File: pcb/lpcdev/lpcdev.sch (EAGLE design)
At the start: 20 parts, among them Q1 16MHz

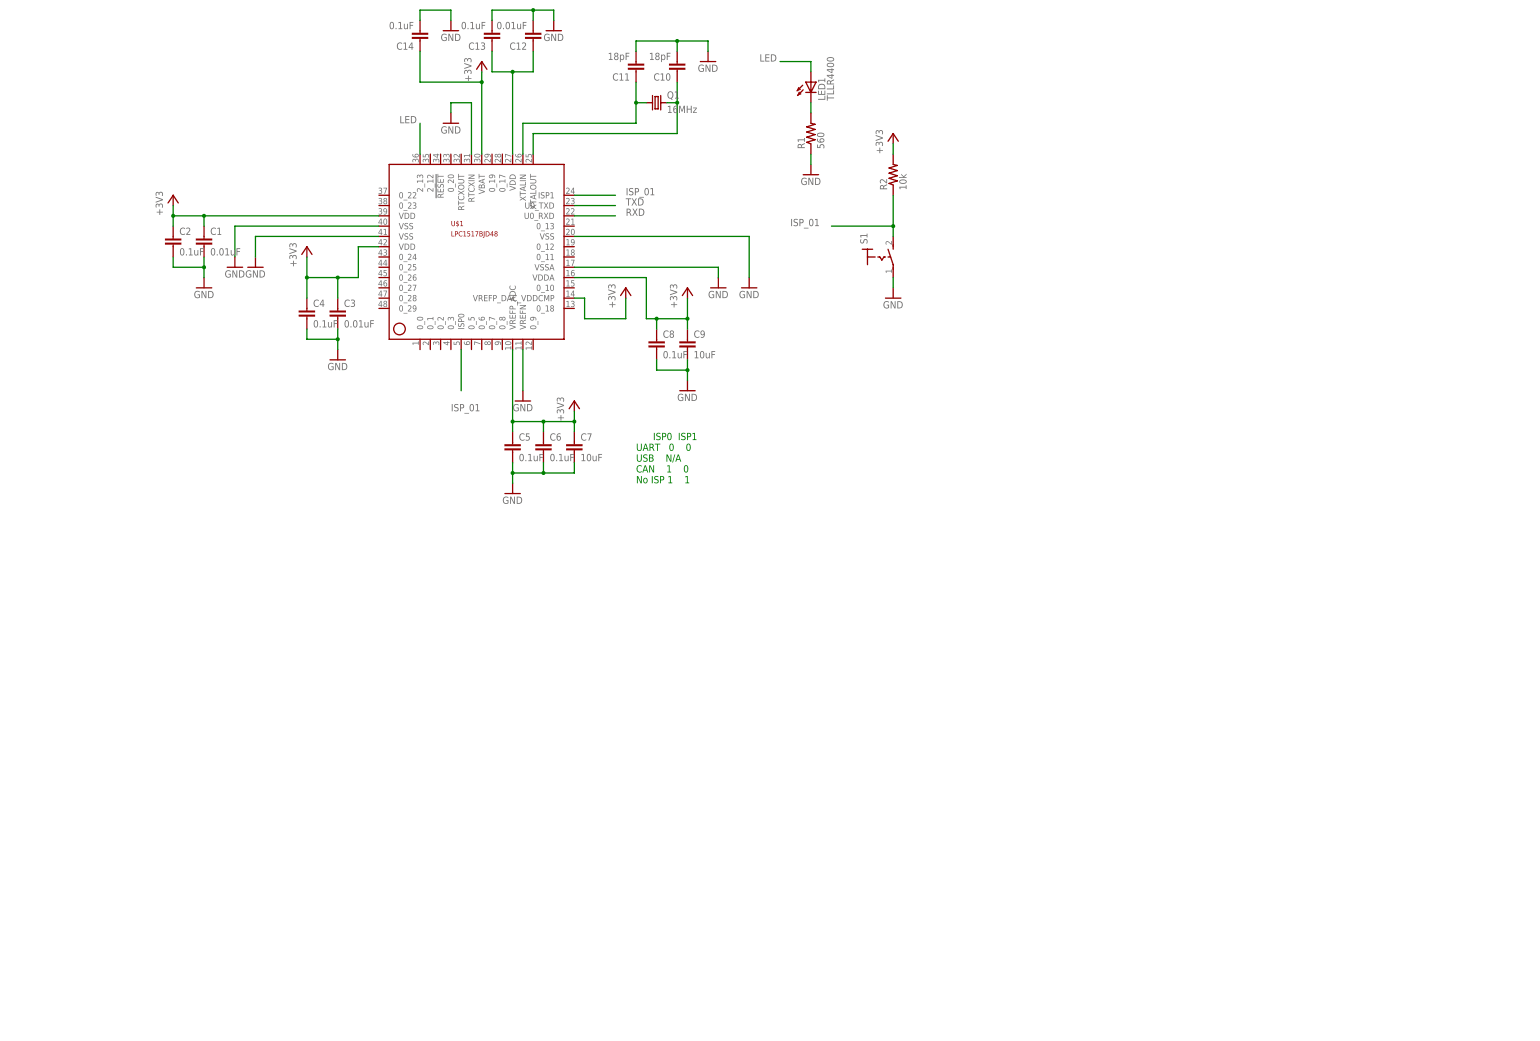
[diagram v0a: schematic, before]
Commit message: Schematic for development board
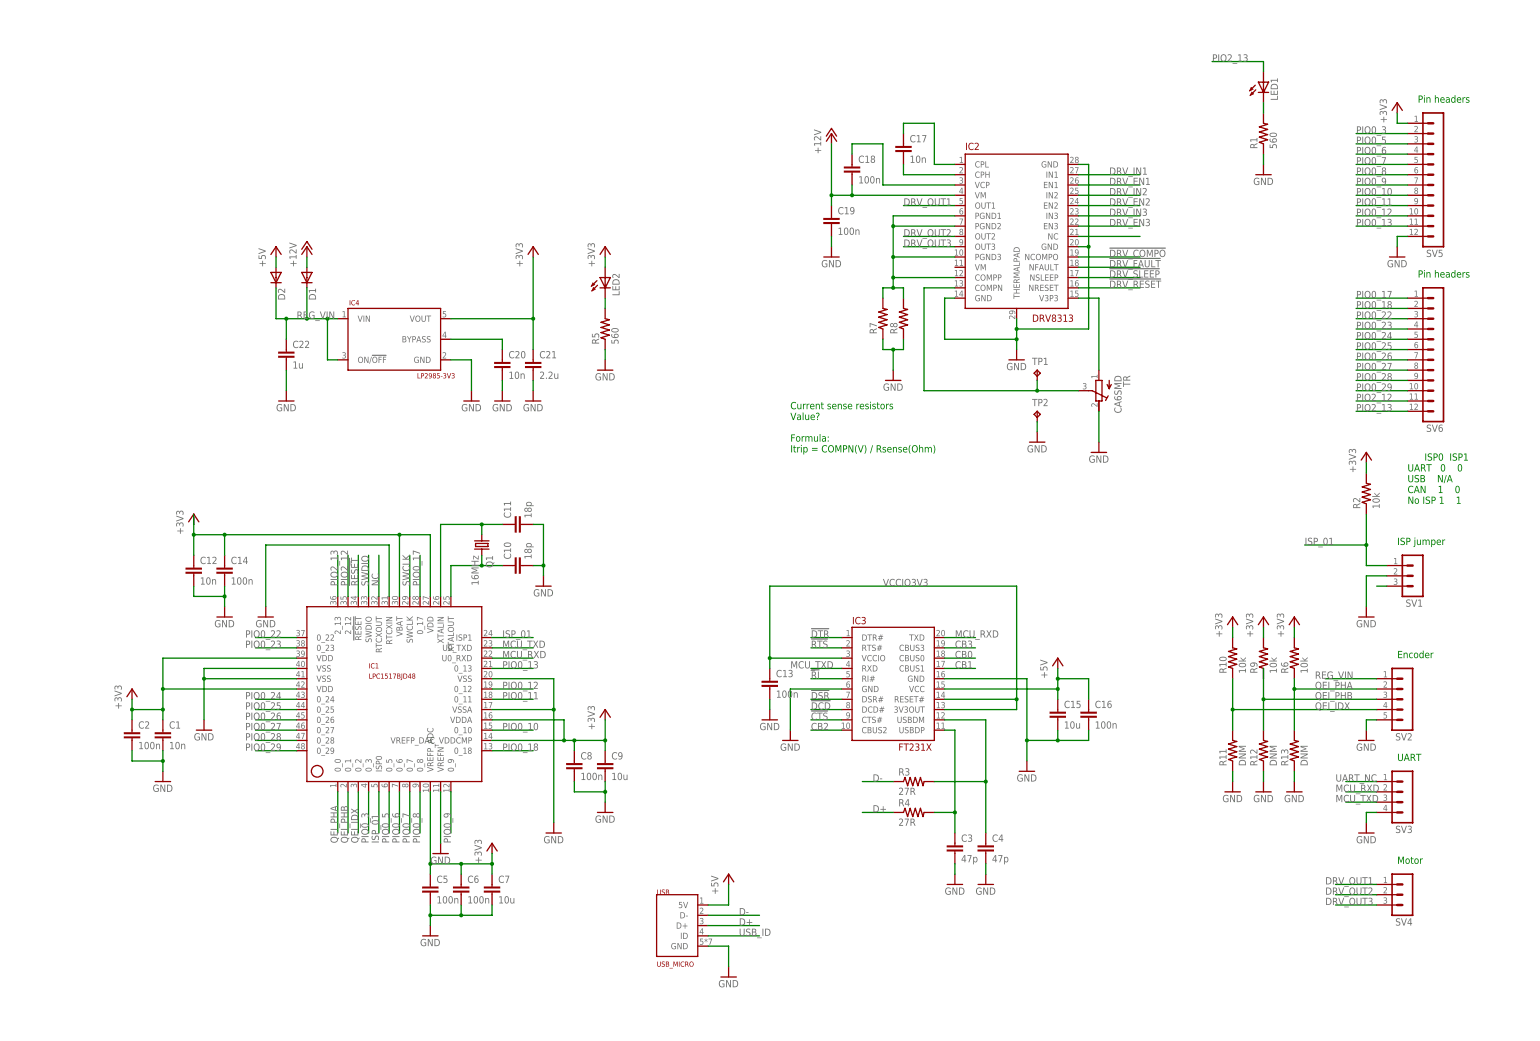
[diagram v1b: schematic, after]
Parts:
- removed S1: (no value), switch:MS243
- removed U$1: LPC1517BJD48, lpclib:LPC1517BJD48
- added C15: 10u, rcl:C-EUC0805
- added C16, C18, C19: 100n, rcl:C-EUC0603
- added C17, C20: 10n, rcl:C-EUC0603
- added C21: 2.2u, rcl:C-EUC0805
- added C22: 1u, rcl:C-EUC0805
- added D1, D2: (no value), diode:DIODE-SOD323-R
- added IC1: LPC1517BJD48, lpclib:LPC1517BJD48
- added IC2: DRV8313, lpclib:DRV8313
- added IC3: FT231X, lpclib:FT231X
- added IC4: LP2985-3V3, lpclib:LP2985-3V3
- added LED2: (no value), led:LEDCHIP-LED0603
- added R10, R6, R9: 10k, rcl:R-US_R0603
- added R11, R12, R13: DNM, rcl:R-US_R0603
- added R3, R4: 27R, rcl:R-US_R0603
- added R5: 560, rcl:R-US_R0603
- added R7, R8: (no value), rcl:R-US_R0805
- added SV1, SV4: (no value), con-lstb:MA03-1
- added SV2: (no value), con-lstb:MA05-1
- added SV3: (no value), con-lstb:MA04-1
- added SV5, SV6: (no value), con-lstb:MA12-1
- added TP1, TP2: TPB1,27, testpad:TPB1,27
- added TR: CA6SMD, lpclib:CA6SMD
- added USB: USB_MICRO, lpclib:USB_MICRO
- C1, C12: value 0.01uF -> 10n; device rcl:C-EUC0805 -> rcl:C-EUC0603
- C10, C11: value 18pF -> 18p; device rcl:C-EUC0805 -> rcl:C-EUC0603
- C13, C14, C2, C5, C6, C8: value 0.1uF -> 100n; device rcl:C-EUC0805 -> rcl:C-EUC0603
- C3: value 0.01uF -> 47p; device rcl:C-EUC0805 -> rcl:C-EUC0603
- C4: value 0.1uF -> 47p; device rcl:C-EUC0805 -> rcl:C-EUC0603
- C7, C9: value 10uF -> 10u
- LED1: value TLLR4400 -> (none); device led:TLLR4400 -> led:LEDCHIP-LED0603
- R1, R2: device rcl:R-US_0207/7 -> rcl:R-US_R0603
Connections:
- net N$1 renamed LED1
- removed net LED: LED1.A, U$1.2_13
- removed net N$15: C10.1, Q1.2, U$1.XTALOUT
- removed net N$16: C11.1, Q1.1, U$1.XTALIN
- removed net N$17: C12.1, C13.1, U$1.VDD@27
- removed net RXD: U$1.U0_RXD
- removed net TXD: U$1.U0_TXD
- new net !CTS: IC3.CTS#
- new net !DCD: IC3.DCD#
- new net !DRV_COMPO: IC2.NCOMPO
- new net !DRV_FAULT: IC2.NFAULT
- new net !DRV_RESET: IC2.NRESET
- new net !DRV_SLEEP: IC2.NSLEEP
- new net !DSR: IC3.DSR#
- new net !DTR: IC3.DTR#
- new net !RESET: IC1.!RESET
- new net !RI: IC3.RI#
- new net !RTS: IC3.RTS#
- new net +12V: C18.2, C19.1, D1.A, IC2.VM@4
- new net +5V: C15.1, C16.1, D2.A, IC3.VCC, USB.5V
- new net CB0: IC3.CBUS0
- new net CB1: IC3.CBUS1
- new net CB2: IC3.CBUS2
- new net CB3: IC3.CBUS3
- new net CRD_VCP: C18.1, IC2.VCP
- new net D+: R4.1, USB.D+
- new net D-: R3.1, USB.D-
- new net DRV_3V3: IC2.V3P3, TR.A
- new net DRV_COMPN: IC2.COMPN, TP1.TP, TR.S
- new net DRV_COMPP: IC2.COMPP, IC2.PGND1, IC2.PGND2, IC2.PGND3, R7.2, R8.2
- new net DRV_CPH: C17.2, IC2.CPH
- new net DRV_CPL: C17.1, IC2.CPL
- new net DRV_EN1: IC2.EN1
- new net DRV_EN2: IC2.EN2
- new net DRV_EN3: IC2.EN3
- new net DRV_IN1: IC2.IN1
- new net DRV_IN2: IC2.IN2
- new net DRV_IN3: IC2.IN3
- new net DRV_NC: IC2.NC
- new net DRV_OUT1: IC2.OUT1, SV4.1
- new net DRV_OUT2: IC2.OUT2, SV4.2
- new net DRV_OUT3: IC2.OUT3, SV4.3
- new net ISP_NC: SV1.3
- new net LED2: LED2.C, R5.2
- new net MCU_RXD: IC1.U0_RXD, IC3.TXD, SV3.2
- new net MCU_TXD: IC1.U0_TXD, IC3.RXD, SV3.3
- new net NC: IC1.RTCXOUT
- new net PIO0_10: IC1.0_10, SV5.8
- new net PIO0_11: IC1.0_11, SV5.9
- new net PIO0_12: IC1.0_12, SV5.10
- new net PIO0_13: IC1.0_13, SV5.11
- new net PIO0_17: IC1.0_17, SV6.1
- new net PIO0_18: IC1.0_18, SV6.2
- new net PIO0_22: IC1.0_22, SV6.3
- new net PIO0_23: IC1.0_23, SV6.4
- new net PIO0_24: IC1.0_24, SV6.5
- new net PIO0_25: IC1.0_25, SV6.6
- new net PIO0_26: IC1.0_26, SV6.7
- new net PIO0_27: IC1.0_27, SV6.8
- new net PIO0_28: IC1.0_28, SV6.9
- new net PIO0_29: IC1.0_29, SV6.10
- new net PIO0_3: IC1.0_3, SV5.2
- new net PIO0_5: IC1.0_5, SV5.3
- new net PIO0_6: IC1.0_6, SV5.4
- new net PIO0_7: IC1.0_7, SV5.5
- new net PIO0_8: IC1.0_8, SV5.6
- new net PIO0_9: IC1.0_9, SV5.7
- new net PIO2_12: IC1.2_12, SV6.11
- new net PIO2_13: IC1.2_13, LED1.A, SV6.12
- new net QEI_IDX: IC1.0_2, R10.1, R11.2, SV2.4
- new net QEI_PHA: IC1.0_0, R13.2, R6.1, SV2.2
- new net QEI_PHB: IC1.0_1, R12.2, R9.1, SV2.3
- new net REG_BYPASS: C20.1, IC4.BYPASS
- new net REG_VIN: C22.1, D1.C, D2.C, IC4.ON/!OFF, IC4.VIN, SV2.1
- new net SWCLK: IC1.SWCLK
- new net SWDIO: IC1.SWDIO
- new net UART_NC: SV3.1
- new net USBDM: C4.1, IC3.USBDM, R3.2
- new net USBDP: C3.1, IC3.USBDP, R4.2
- new net USB_ID: USB.ID
- new net VCCIO3V3: C13.1, IC3.3V3OUT, IC3.RESET#, IC3.VCCIO
- new net XTALIN: C11.1, IC1.XTALIN, Q1.1
- new net XTALOUT: C10.1, IC1.XTALOUT, Q1.2
- net +3V3: now also C12.1, C21.1, IC1.VBAT, IC1.VDD@27, IC1.VDD@39, IC1.VDD@42, IC1.VDDA, IC1.VREFP_ADC, IC1.VREFP_DAC_VDDCMP, IC4.VOUT, LED2.A, R10.2, R6.2, R9.2, SV5.1; no longer C3.1, C4.1, U$1.VBAT, U$1.VDD@39, U$1.VDD@42, U$1.VDDA, U$1.VREFP_ADC, U$1.VREFP_DAC_VDDCMP
- net GND: now also C15.2, C16.2, C19.2, C20.2, C21.2, C22.2, IC1.RTCXIN, IC1.VREFN, IC1.VSS@20, IC1.VSS@40, IC1.VSS@41, IC1.VSSA, IC2.GND@14, IC2.GND@20, IC2.GND@28, IC2.THERMALPAD, IC3.GND@16, IC3.GND@6, IC4.GND, R11.1, R12.1, R13.1, R5.1, R7.1, R8.1, SV1.2, SV2.5, SV3.4, SV5.12, TP2.TP, TR.E, USB.GND; no longer S1.P, U$1.RTCXIN, U$1.VREFN, U$1.VSS@20, U$1.VSS@40, U$1.VSS@41, U$1.VSSA
- net ISP_01: now also IC1.ISP0, IC1.ISP1, SV1.1; no longer S1.S, U$1.ISP0, U$1.ISP1
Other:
- note added: "Current sense resistors Value? Formula: Itrip = COMPN(V) / Rsense(Ohm)"
- note added: "Encoder"
- note added: "ISP jumper"
- note added: "Motor"
- note added: "Pin headers"
- note added: "UART"
- moved on the sheet: C1, C10, C11, C12, C13, C14, C2, C3, C4, C5, C6, C7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

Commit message: Added two more motor drivers, named nets and made first pass on board placement
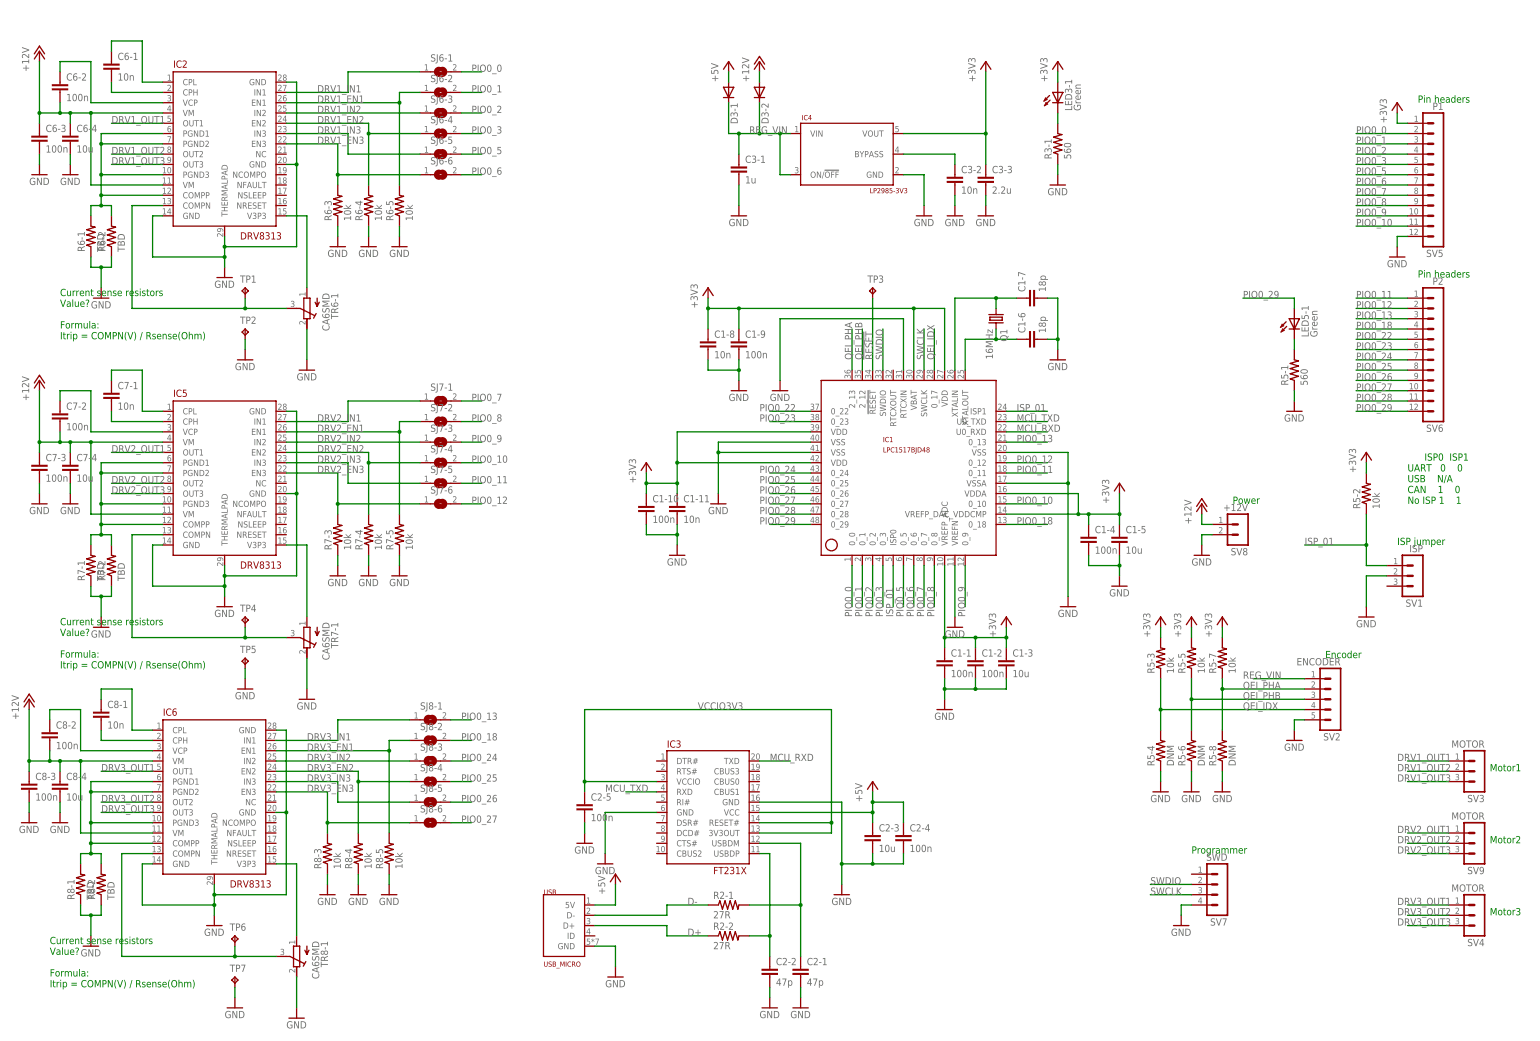
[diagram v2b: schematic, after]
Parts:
- removed C1, C12, C17, C20: 10n, rcl:C-EUC0603
- removed C10, C11: 18p, rcl:C-EUC0603
- removed C13, C14, C16, C18, C19, C2, C5, C6, C8: 100n, rcl:C-EUC0603
- removed C15, C7, C9: 10u, rcl:C-EUC0805
- removed C21: 2.2u, rcl:C-EUC0805
- removed C22: 1u, rcl:C-EUC0805
- removed C3, C4: 47p, rcl:C-EUC0603
- removed D1, D2: (no value), diode:DIODE-SOD323-R
- removed LED1, LED2: (no value), led:LEDCHIP-LED0603
- removed R1, R5: 560, rcl:R-US_R0603
- removed R10, R6, R9: 10k, rcl:R-US_R0603
- removed R11, R12, R13: DNM, rcl:R-US_R0603
- removed R3, R4: 27R, rcl:R-US_R0603
- removed R7, R8: (no value), rcl:R-US_R0805
- removed TR: CA6SMD, lpclib:CA6SMD
- added C1-1, C1-10, C1-2, C1-4, C1-9, C2-4, C2-5, C6-2, C6-3, C7-2, C7-3, C8-2, C8-3: 100n, rcl:C-EUC0603
- added C1-11, C1-8, C3-2, C6-1, C7-1, C8-1: 10n, rcl:C-EUC0603
- added C1-3, C1-5, C2-3, C6-4, C7-4, C8-4: 10u, rcl:C-EUC0805
- added C1-6, C1-7: 18p, rcl:C-EUC0603
- added C2-1, C2-2: 47p, rcl:C-EUC0603
- added C3-1: 1u, rcl:C-EUC0805
- added C3-3: 2.2u, rcl:C-EUC0805
- added D3-1, D3-2: (no value), diode:DIODE-SOD323-R
- added IC5, IC6: DRV8313, lpclib:DRV8313
- added LED3-1, LED5-1: Green, led:LEDCHIP-LED0603
- added R2-1, R2-2: 27R, rcl:R-US_R0603
- added R3-1, R5-1: 560, rcl:R-US_R0603
- added R5-3, R5-5, R5-7, R6-3, R6-4, R6-5, R7-3, R7-4, R7-5, R8-3, R8-4, R8-5: 10k, rcl:R-US_R0603
- added R5-4, R5-6, R5-8: DNM, rcl:R-US_R0603
- added R6-1, R6-2, R7-1, R7-2, R8-1, R8-2: TBD, rcl:R-US_R0805
- added SJ6-1, SJ6-2, SJ6-3, SJ6-4, SJ6-5, SJ6-6, SJ7-1, SJ7-2, SJ7-3, SJ7-4, SJ7-5, SJ7-6, SJ8-1, SJ8-2, SJ8-3, SJ8-4, SJ8-5, SJ8-6: (no value), jumper:SJ
- added SV7: SWD, con-lstb:MA04-1
- added SV8: +12V, lpclib:MA02-1
- added SV9: MOTOR, con-lstb:MA03-1
- added TP3, TP4, TP5, TP6, TP7: TPB1,27, testpad:TPB1,27
- added TR6-1, TR7-1, TR8-1: CA6SMD, lpclib:CA6SMD
- SV1: value (none) -> ISP
- SV2: value (none) -> ENCODER
- SV3: value (none) -> MOTOR; device con-lstb:MA04-1 -> con-lstb:MA03-1
- SV4: value (none) -> MOTOR
- SV5: value (none) -> P1
- SV6: value (none) -> P2
- renumbered R2 to R5-2
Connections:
- removed net !CTS: IC3.CTS#
- removed net !DCD: IC3.DCD#
- removed net !DRV_COMPO: IC2.NCOMPO
- removed net !DRV_FAULT: IC2.NFAULT
- removed net !DRV_RESET: IC2.NRESET
- removed net !DRV_SLEEP: IC2.NSLEEP
- removed net !DSR: IC3.DSR#
- removed net !DTR: IC3.DTR#
- removed net !RI: IC3.RI#
- removed net !RTS: IC3.RTS#
- removed net CB0: IC3.CBUS0
- removed net CB1: IC3.CBUS1
- removed net CB2: IC3.CBUS2
- removed net CB3: IC3.CBUS3
- removed net CRD_VCP: C18.1, IC2.VCP
- removed net DRV_3V3: IC2.V3P3, TR.A
- removed net DRV_COMPN: IC2.COMPN, TP1.TP, TR.S
- removed net DRV_COMPP: IC2.COMPP, IC2.PGND1, IC2.PGND2, IC2.PGND3, R7.2, R8.2
- removed net DRV_CPH: C17.2, IC2.CPH
- removed net DRV_CPL: C17.1, IC2.CPL
- removed net DRV_EN1: IC2.EN1
- removed net DRV_EN2: IC2.EN2
- removed net DRV_EN3: IC2.EN3
- removed net DRV_IN1: IC2.IN1
- removed net DRV_IN2: IC2.IN2
- removed net DRV_IN3: IC2.IN3
- removed net DRV_NC: IC2.NC
- removed net DRV_OUT1: IC2.OUT1, SV4.1
- removed net DRV_OUT2: IC2.OUT2, SV4.2
- removed net DRV_OUT3: IC2.OUT3, SV4.3
- removed net ISP_NC: SV1.3
- removed net NC: IC1.RTCXOUT
- removed net PIO0_17: IC1.0_17, SV6.1
- removed net PIO2_12: IC1.2_12, SV6.11
- removed net PIO2_13: IC1.2_13, LED1.A, SV6.12
- removed net UART_NC: SV3.1
- removed net USB_ID: USB.ID
- new net DRV1_3V3: IC2.V3P3, TR6-1.A
- new net DRV1_COMPN: IC2.COMPN, TP1.TP, TR6-1.S
- new net DRV1_COMPP: IC2.COMPP, IC2.PGND1, IC2.PGND2, IC2.PGND3, R6-1.2, R6-2.2
- new net DRV1_CPH: C6-1.2, IC2.CPH
- new net DRV1_CPL: C6-1.1, IC2.CPL
- new net DRV1_EN1: IC2.EN1, R6-5.2, SJ6-2.1
- new net DRV1_EN2: IC2.EN2, R6-4.2, SJ6-4.1
- new net DRV1_EN3: IC2.EN3, R6-3.2, SJ6-6.1
- new net DRV1_IN1: IC2.IN1, SJ6-1.1
- new net DRV1_IN2: IC2.IN2, SJ6-3.1
- new net DRV1_IN3: IC2.IN3, SJ6-5.1
- new net DRV1_OUT1: IC2.OUT1, SV3.1
- new net DRV1_OUT2: IC2.OUT2, SV3.2
- new net DRV1_OUT3: IC2.OUT3, SV3.3
- new net DRV1_VCP: C6-2.1, IC2.VCP
- new net DRV2_3V1: IC5.V3P3, TR7-1.A
- new net DRV2_COMPN1: IC5.COMPN, TP4.TP, TR7-1.S
- new net DRV2_COMPP1: IC5.COMPP, IC5.PGND1, IC5.PGND2, IC5.PGND3, R7-1.2, R7-2.2
- new net DRV2_CPH1: C7-1.2, IC5.CPH
- new net DRV2_CPL1: C7-1.1, IC5.CPL
- new net DRV2_EN1: IC5.EN1, R7-5.2, SJ7-2.1
- new net DRV2_EN2: IC5.EN2, R7-4.2, SJ7-4.1
- new net DRV2_EN3: IC5.EN3, R7-3.2, SJ7-6.1
- new net DRV2_IN1: IC5.IN1, SJ7-1.1
- new net DRV2_IN2: IC5.IN2, SJ7-3.1
- new net DRV2_IN3: IC5.IN3, SJ7-5.1
- new net DRV2_OUT1: IC5.OUT1, SV9.1
- new net DRV2_OUT2: IC5.OUT2, SV9.2
- new net DRV2_OUT3: IC5.OUT3, SV9.3
- new net DRV2_VCP1: C7-2.1, IC5.VCP
- new net DRV3_3V2: IC6.V3P3, TR8-1.A
- new net DRV3_COMPN2: IC6.COMPN, TP6.TP, TR8-1.S
- new net DRV3_COMPP2: IC6.COMPP, IC6.PGND1, IC6.PGND2, IC6.PGND3, R8-1.2, R8-2.2
- new net DRV3_CPH2: C8-1.2, IC6.CPH
- new net DRV3_CPL2: C8-1.1, IC6.CPL
- new net DRV3_EN1: IC6.EN1, R8-5.2, SJ8-2.1
- new net DRV3_EN2: IC6.EN2, R8-4.2, SJ8-4.1
- new net DRV3_EN3: IC6.EN3, R8-3.2, SJ8-6.1
- new net DRV3_IN1: IC6.IN1, SJ8-1.1
- new net DRV3_IN2: IC6.IN2, SJ8-3.1
- new net DRV3_IN3: IC6.IN3, SJ8-5.1
- new net DRV3_OUT1: IC6.OUT1, SV4.1
- new net DRV3_OUT2: IC6.OUT2, SV4.2
- new net DRV3_OUT3: IC6.OUT3, SV4.3
- new net DRV3_VCP2: C8-2.1, IC6.VCP
- new net PIO0_0: IC1.0_0, SJ6-1.2, SV5.2
- new net PIO0_1: IC1.0_1, SJ6-2.2, SV5.3
- new net PIO0_2: IC1.0_2, SJ6-3.2, SV5.4
- net !RESET: now also TP3.TP
- net +12V: now also C6-2.2, C6-3.1, C6-4.1, C7-2.2, C7-3.1, C7-4.1, C8-2.2, C8-3.1, C8-4.1, D3-2.A, IC2.VM@11, IC5.VM@11, IC5.VM@4, IC6.VM@11, IC6.VM@4, SV8.1; no longer C18.2, C19.1, D1.A
- net +3V3: now also C1-1.1, C1-10.1, C1-11.1, C1-2.1, C1-3.1, C1-4.1, C1-5.1, C1-8.1, C1-9.1, C3-3.1, LED3-1.A, R5-3.2, R5-5.2, R5-7.2; no longer C1.1, C12.1, C14.1, C2.1, C21.1, C5.1, C6.1, C7.1, C8.1, C9.1, LED2.A, R10.2, R6.2, R9.2
- net +5V: now also C2-3.1, C2-4.1, D3-1.A; no longer C15.1, C16.1, D2.A
- net D+: now also R2-2.1; no longer R4.1
- net D-: now also R2-1.1; no longer R3.1
- net GND: now also C1-1.2, C1-10.2, C1-11.2, C1-2.2, C1-3.2, C1-4.2, C1-5.2, C1-6.2, C1-7.2, C1-8.2, C1-9.2, C2-1.2, C2-2.2, C2-3.2, C2-4.2, C2-5.2, C3-1.2, C3-2.2, C3-3.2, C6-3.2, C6-4.2, C7-3.2, C7-4.2, C8-3.2, C8-4.2, IC5.GND@14, IC5.GND@20, IC5.GND@28, IC5.THERMALPAD, IC6.GND@14, IC6.GND@20, IC6.GND@28, IC6.THERMALPAD, R3-1.1, R5-1.1, R5-4.1, R5-6.1, R5-8.1, R6-1.1, R6-2.1, R6-3.1, R6-4.1, R6-5.1, R7-1.1, R7-2.1, R7-3.1, R7-4.1, R7-5.1, R8-1.1, R8-2.1, R8-3.1, R8-4.1, R8-5.1, SV7.4, SV8.2, TP5.TP, TP7.TP, TR6-1.E, TR7-1.E, TR8-1.E; no longer C1.2, C10.2, C11.2, C12.2, C13.2, C14.2, C15.2, C16.2, C19.2, C2.2, C20.2, C21.2, C22.2, C3.2, C4.2, C5.2, C6.2, C7.2, C8.2, C9.2, R1.1, R11.1, R12.1, R13.1, R5.1, R7.1, R8.1, SV3.4, TR.E
- net LED1: now also LED5-1.C, R5-1.2; no longer LED1.C, R1.2
- net LED2: now also LED3-1.C, R3-1.2; no longer LED2.C, R5.2
- net MCU_RXD: no longer SV3.2
- net MCU_TXD: no longer SV3.3
- net PIO0_10: now also SJ7-4.2, SV5.11; no longer SV5.8
- net PIO0_11: now also SJ7-5.2, SV6.1; no longer SV5.9
- net PIO0_12: now also SJ7-6.2, SV6.2; no longer SV5.10
- net PIO0_13: now also SJ8-1.2, SV6.3; no longer SV5.11
- net PIO0_18: now also SJ8-2.2, SV6.4; no longer SV6.2
- net PIO0_22: now also SV6.5; no longer SV6.3
- net PIO0_23: now also SV6.6; no longer SV6.4
- net PIO0_24: now also SJ8-3.2, SV6.7; no longer SV6.5
- net PIO0_25: now also SJ8-4.2, SV6.8; no longer SV6.6
- net PIO0_26: now also SJ8-5.2, SV6.9; no longer SV6.7
- net PIO0_27: now also SJ8-6.2, SV6.10; no longer SV6.8
- net PIO0_28: now also SV6.11; no longer SV6.9
- net PIO0_29: now also LED5-1.A, SV6.12; no longer SV6.10
- net PIO0_3: now also SJ6-4.2, SV5.5; no longer SV5.2
- net PIO0_5: now also SJ6-5.2, SV5.6; no longer SV5.3
- net PIO0_6: now also SJ6-6.2, SV5.7; no longer SV5.4
- net PIO0_7: now also SJ7-1.2, SV5.8; no longer SV5.5
- net PIO0_8: now also SJ7-2.2, SV5.9; no longer SV5.6
- net PIO0_9: now also SJ7-3.2, SV5.10; no longer SV5.7
- net QEI_IDX: now also IC1.0_17, R5-3.1, R5-4.2; no longer IC1.0_2, R10.1, R11.2
- net QEI_PHA: now also IC1.2_13, R5-7.1, R5-8.2; no longer IC1.0_0, R13.2, R6.1
- net QEI_PHB: now also IC1.2_12, R5-5.1, R5-6.2; no longer IC1.0_1, R12.2, R9.1
- net REG_BYPASS: now also C3-2.1; no longer C20.1
- net REG_VIN: now also C3-1.1, D3-1.C, D3-2.C; no longer C22.1, D1.C, D2.C
- net SWCLK: now also SV7.3
- net SWDIO: now also SV7.2
- net USBDM: now also C2-1.1, R2-1.2; no longer C4.1, R3.2
- net USBDP: now also C2-2.1, R2-2.2; no longer C3.1, R4.2
- net VCCIO3V3: now also C2-5.1; no longer C13.1
- net XTALIN: now also C1-7.1; no longer C11.1
- net XTALOUT: now also C1-6.1; no longer C10.1
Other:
- note added: "Motor1"
- note added: "Motor2"
- note added: "Motor3"
- note added: "Power"
- note added: "Programmer"
- note removed: "Motor"
- note removed: "UART"
- moved on the sheet: IC1, IC2, IC3, IC4, Q1, SV2, SV4, TP1, TP2, USB
